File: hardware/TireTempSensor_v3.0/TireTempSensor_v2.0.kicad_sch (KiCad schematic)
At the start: 36 parts, among them J1 SWD_01x06, J2 CAN_01x04, SW1 RESET, SW2 3 pos dip switch, U1 STM32G0C1KCTxN, Y1 16MGHz

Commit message: Piotruś prosił :3
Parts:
- removed J1: SWD_01x06, Connector_PinHeader_2.54mm:PinHeader_1x06_P2.54mm_Vertical, symbol Connector_Generic:Conn_01x06
- added J3: FTSH-107-01-L-D-K, Samacsys:FTSH-107-XX-YYY-D-K, symbol Samacsys_kicad_sym:FTSH-107-01-L-D-K
- D1: value D_Zener -> 30V; footprint (none) -> Diode_SMD:D_SOD-123
- D10, D7, D8, D9: footprint (none) -> Package_TO_SOT_SMD:SOT-23_Handsoldering
- D11, D12: footprint (none) -> Diode_SMD:D_SOD-123
- SW2: footprint (none) -> footprint:DS04254103BKSMT
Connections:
- net GND: now also J3.11 (Pin_11), J3.5 (Pin_5), J3.7 (Pin_7); no longer D9.3 (common)
- net NRST: now also J3.12 (Pin_12)
- net SWCLK: now also J3.6 (Pin_6)
- net SWDIO: now also J3.4 (Pin_4)
- net SWO: now also J3.8 (Pin_8)
- new net +3.3V: J3.3 (Pin_3)
- new net GND_ISO: D9.3 (common)
- no-connect marks 1 -> 6
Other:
- moved on the sheet: J2

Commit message: Poprawki, kontynuacja layoutu
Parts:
- removed C16: 100n, Capacitor_SMD:C_0603_1608Metric, symbol Device:C_Small
- removed D10, D7, D8, D9: D_TVS_Dual_AAC, Package_TO_SOT_SMD:SOT-23_Handsoldering, symbol Device:D_TVS_Dual_AAC
- removed R17: 10k, Resistor_SMD:R_0603_1608Metric, symbol Device:R_Small_US
- removed R20: 1k, Resistor_SMD:R_0603_1608Metric, symbol Device:R_Small_US
- removed SW2: 3 pos dip switch, footprint:DS04254103BKSMT, symbol Switch:SW_DIP_x03
- added SW3: SW_DIP_x02, footprint:2192LPST, symbol Switch:SW_DIP_x02
- J2: value CAN_01x04 -> Main connector; footprint Connector_Wire:SolderWire-0.1sqmm_1x04_P3.6mm_D0.4mm_OD1mm_Relief -> footprint:M80-51004YY
- J3: footprint Samacsys:FTSH-107-XX-YYY-D-K -> footprint:FTSH-107-XX-YYY-DV-K
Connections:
- net Switch3 is gone; now on net CAN RX: U1.22 (PA11/PA9)
- net CAN +: now also J2.4 (Pin_4); no longer J2.3 (Pin_3)
- net CAN -: now also J2.3 (Pin_3); no longer J2.4 (Pin_4)
- net CAN TX: now also U1.1 (PB9)
- net LED ERR: now also U1.11 (PA4); no longer U1.13 (PA6)
- net LED OK: now also U1.10 (PA3); no longer U1.12 (PA5)
- net LED WAR1: now also U1.12 (PA5); no longer U1.14 (PA7)
- net LED WAR2: now also U1.13 (PA6); no longer U1.18 (PA8)
- net Switch1: now also SW3.1
- net Switch2: now also SW3.2
- net at R19.1: now also SW3.3
- net at R18.1: now also SW3.4
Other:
- added sheet ESD_Protection (ESD_Protection.kicad_sch)
- note added: "Dla 4 czujników wystarczą 2 pozycje adresy 0-3"
- note removed: "ESD Protection"
- moved on the sheet: C12, C13, J2, R15, R16, R18, R19, U1

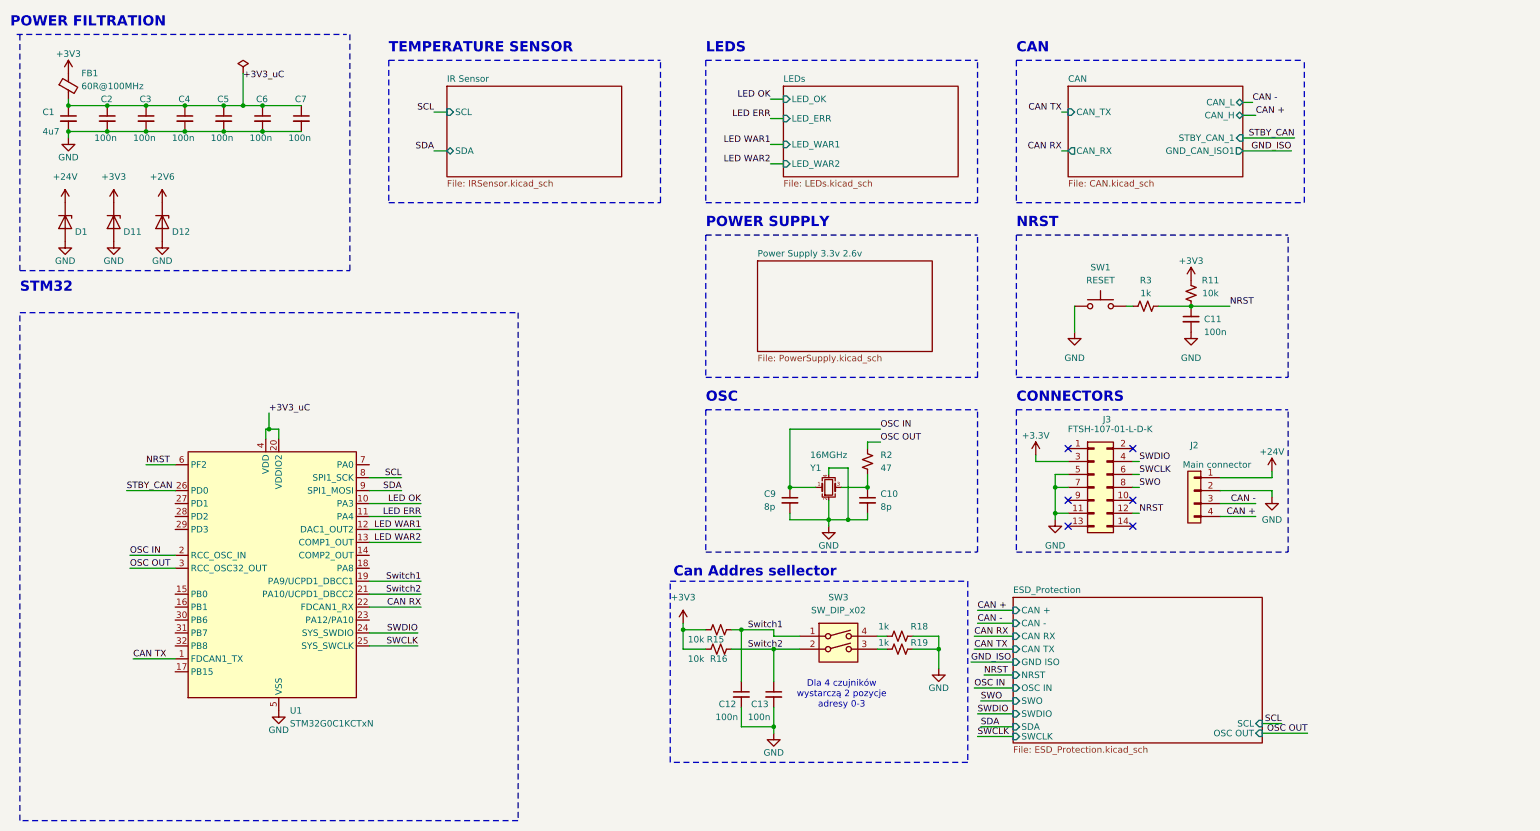
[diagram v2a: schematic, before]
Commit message: Nowy layout, nowe tvsy
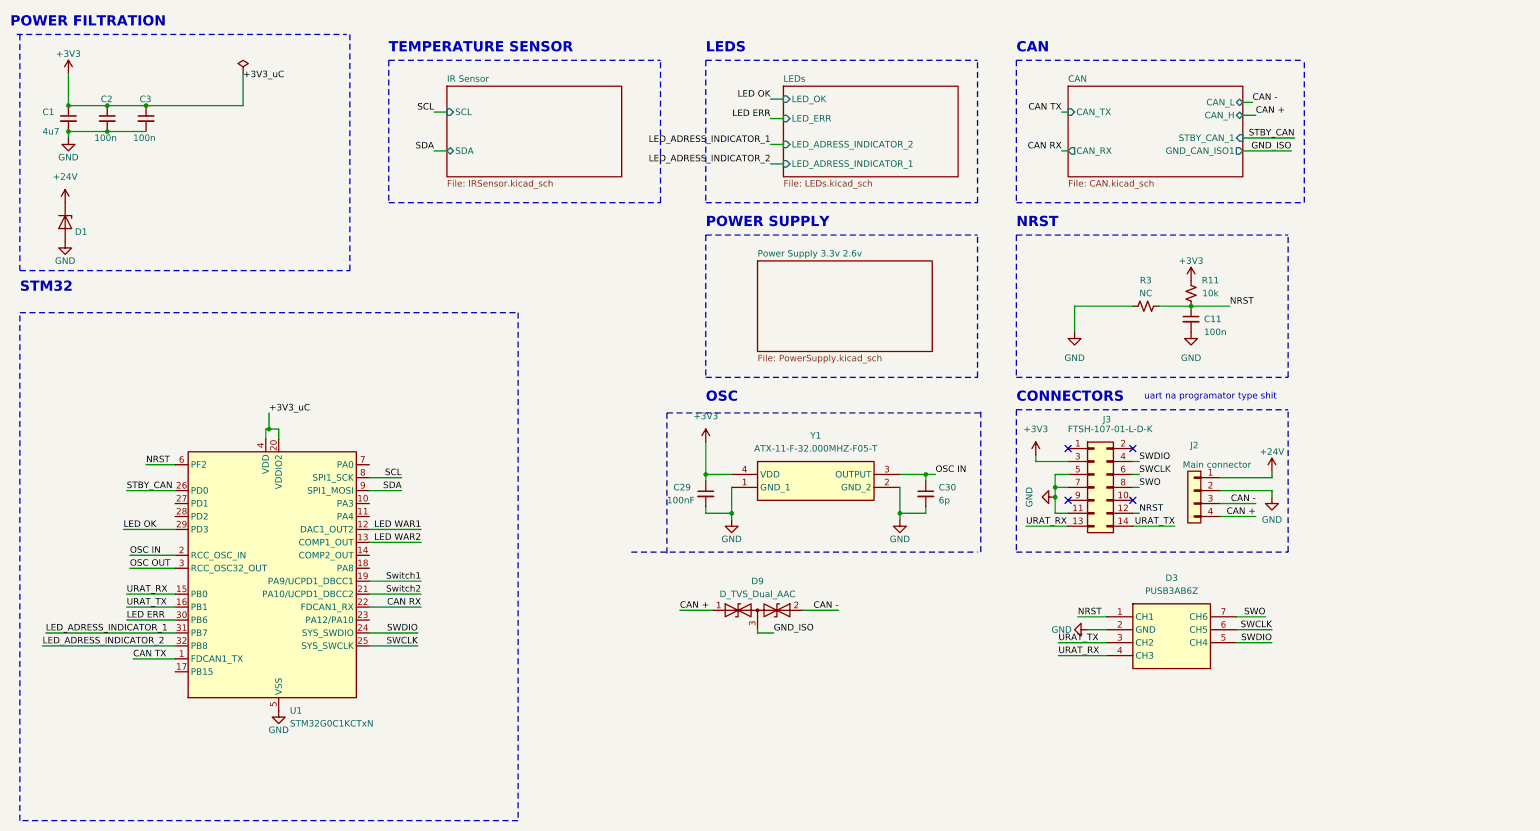
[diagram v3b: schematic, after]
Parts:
- removed C10, C9: 8p, Capacitor_SMD:C_0603_1608Metric, symbol Device:C_Small
- removed C12, C13, C4, C5, C6, C7: 100n, Capacitor_SMD:C_0603_1608Metric, symbol Device:C_Small
- removed D11, D12: D_Zener, Diode_SMD:D_SOD-123, symbol Device:D_Zener
- removed FB1: 60R@100MHz, Inductor_SMD:L_0603_1608Metric, symbol Device:FerriteBead_Small
- removed R15, R16: 10k, Resistor_SMD:R_0603_1608Metric, symbol Device:R_Small_US
- removed R18, R19: 1k, Resistor_SMD:R_0603_1608Metric, symbol Device:R_Small_US
- removed R2: 47, Resistor_SMD:R_0603_1608Metric, symbol Device:R_Small_US
- removed SW1: RESET, Button:PTS815SJK250SMTRLFS, symbol Switch:SW_MEC_5G
- removed SW3: SW_DIP_x02, footprint:2192LPST, symbol Switch:SW_DIP_x02
- removed Y1: 16MGHz, Crystal:Crystal_SMD_SeikoEpson_TSX3225-4Pin_3.2x2.5mm, symbol Device:Crystal_GND24_Small
- added C29: 100nF, Capacitor_SMD:C_0603_1608Metric_Pad1.08x0.95mm_HandSolder, symbol Device:C_Small
- added C30: 6p, Capacitor_SMD:C_0603_1608Metric_Pad1.08x0.95mm_HandSolder, symbol Device:C_Small
- added D3: PUSB3AB6Z, footprint:PUSB3AB6Z, symbol PUSB3AB6Z:PUSB3AB6Z
- added D9: D_TVS_Dual_AAC, Package_TO_SOT_SMD:SOT-23_Handsoldering, symbol Device:D_TVS_Dual_AAC
- added Y1: ATX-11-F-32.000MHZ-F05-T, footprint:ATX11F32000MHZF05T, symbol Samacsys:ATX-11-F-32.000MHZ-F05-T
- R3: value 1k -> NC; footprint Resistor_SMD:R_0603_1608Metric -> Resistor_SMD:R_0201_0603Metric
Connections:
- net +3.3V is gone; now on net +3V3: J3.3 (Pin_3)
- net +3V3_uC is gone; now on net +3V3: C1.1, C2.1, C3.1, U1.20 (VDDIO2), U1.4 (VDD)
- net +3V3: now also C29.1, Y1.4 (VDD)
- net CAN +: now also D9.1 (A1)
- net CAN -: now also D9.2 (A2)
- net GND: now also R3.1, C29.2, C30.2, D3.2 (GND), Y1.1 (GND_1), Y1.2 (GND_2)
- net GND_ISO: now also D9.3 (common)
- net LED ERR: now also U1.30 (PB6); no longer U1.11 (PA4)
- net LED OK: now also U1.29 (PD3); no longer U1.10 (PA3)
- net NRST: now also D3.1 (CH1)
- net OSC IN: now also C30.1, Y1.3 (OUTPUT)
- net SWCLK: now also D3.6 (CH5)
- net SWDIO: now also D3.5 (CH4)
- net SWO: now also D3.7 (CH6)
- net URAT_RX: now reaches U1.15 (PB0)
- net URAT_RX: now also J3.13 (Pin_13), D3.4 (CH3)
- net URAT_TX: now reaches U1.16 (PB1)
- net URAT_TX: now also J3.14 (Pin_14), D3.3 (CH2)
- net LED_ADRESS_INDICATOR_1: now reaches U1.31 (PB7)
- net LED_ADRESS_INDICATOR_2: now reaches U1.32 (PB8)
- no-connect marks 6 -> 4
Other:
- removed sheet ESD_Protection
- sheet LEDs ports: added LED_ADRESS_INDICATOR_1, LED_ADRESS_INDICATOR_2; removed LED_WAR1, LED_WAR2
- note added: "uart na programator type shit"
- note removed: "Can Addres sellector"
- note removed: "Dla 4 czujników wystarczą 2 pozycje adresy 0-3"

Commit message: Gotowe do sprawdzenia
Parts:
- R3: footprint Resistor_SMD:R_0201_0603Metric -> Resistor_SMD:R_0402_1005Metric
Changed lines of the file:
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@@
 			)
 		)
-		(property "Footprint" "Resistor_SMD:R_0201_0603Metric"
+		(property "Footprint" "Resistor_SMD:R_0402_1005Metric"
 			(at 248.92 73.66 0)
 			(effects

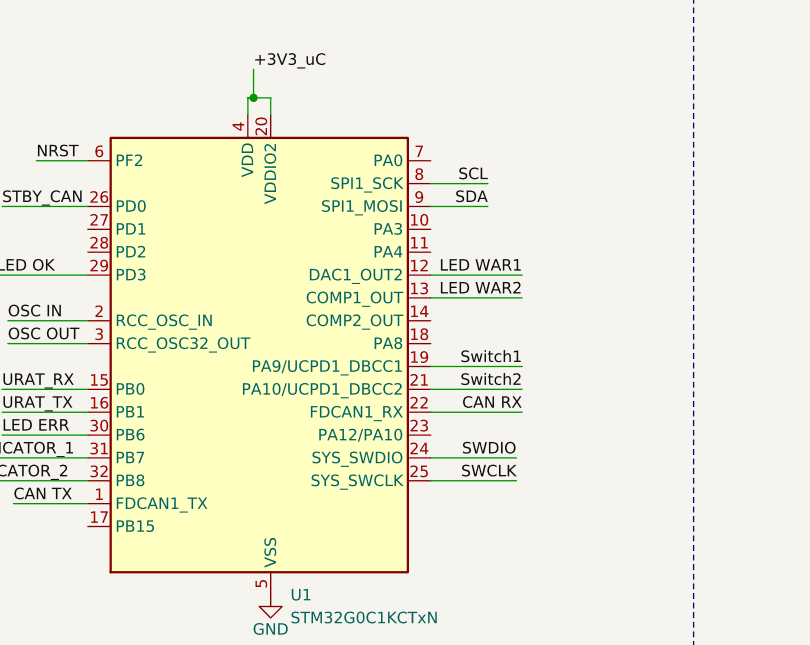
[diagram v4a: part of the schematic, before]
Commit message: Poprawiono SPI NA I2C
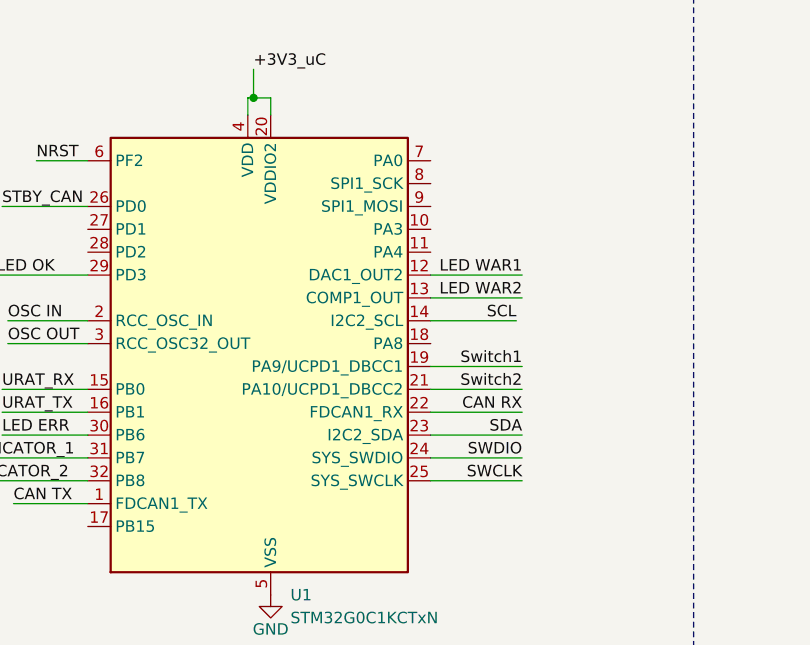
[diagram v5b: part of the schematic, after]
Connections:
- net SCL: now also U1.14 (PA7); no longer U1.8 (PA1)
- net SDA: now also U1.23 (PA12/PA10); no longer U1.9 (PA2)
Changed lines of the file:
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@@
 	(wire
 		(pts
-			(xy 96.52 137.795) (xy 106.045 137.795)
-		)
-		(stroke
-			(width 0)
-			(type default)
-		)
-	)
-	(wire
-		(pts
-			(xy 96.52 107.315) (xy 102.87 107.315)
+			(xy 96.52 137.795) (xy 106.68 137.795)
 		)
 		(stroke
@@
 	(wire
 		(pts
+			(xy 96.52 122.555) (xy 106.045 122.555)
+		)
+		(stroke
+			(width 0)
+			(type default)
+		)
+	)
+	(wire
+		(pts
 			(xy 246.38 114.3) (xy 247.65 114.3)
 		)
@@
 		)
 	)
+	(wire
+		(pts
+			(xy 96.52 135.255) (xy 106.68 135.255)
+		)
+		(stroke
+			(width 0)
+			(type default)
+		)
+	)
 	(polyline
 		(pts
@@
 	(wire
 		(pts
-			(xy 96.52 140.335) (xy 106.045 140.335)
+			(xy 96.52 140.335) (xy 106.68 140.335)
 		)
 		(stroke
@@
 		(pts
 			(xy 172.72 137.795) (xy 172.72 137.16)
-		)
-		(stroke
-			(width 0)
-			(type default)
-		)
-	)
-	(wire
-		(pts
-			(xy 96.52 109.855) (xy 102.87 109.855)
 		)
 		(stroke
@@
 	)
 	(label "SWCLK"
-		(at 106.045 140.335 180)
+		(at 106.68 140.335 180)
 		(effects
 			(font
@@
 	)
 	(label "SDA"
-		(at 102.87 109.855 180)
+		(at 106.68 135.255 180)
 		(effects
 			(font
@@
 	)
 	(label "SCL"
-		(at 102.87 107.315 180)
+		(at 106.045 122.555 180)
 		(effects
 			(font
@@
 	)
 	(label "SWDIO"
-		(at 106.045 137.795 180)
+		(at 106.68 137.795 180)
 		(effects
 			(font
@@
 		)
 		(pin "14"
-			(alternate "COMP2_OUT")
+			(alternate "I2C2_SCL")
 		)
 		(pin "23"
+			(alternate "I2C2_SDA")
 		)
 		(pin "2"

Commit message: Poprawione :3
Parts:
- added D7, D8: Quad TVS, SOT95P285X140-6N, symbol D5V0P4UR6SO-7:D5V0P4UR6SO-7
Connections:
- net +3V3: now also D8.3 (I/O2)
- net GND: now also D7.2 (VSS), D7.5 (VCC), D8.2 (VSS), D8.5 (VCC); no longer D3.2 (GND)
- net NRST: now also D7.1 (I/O1); no longer D3.1 (CH1)
- net SWCLK: now also D7.6 (I/O4); no longer D3.6 (CH5)
- net SWDIO: now also D7.4 (I/O3); no longer D3.5 (CH4)
- net SWO: now also D7.3 (I/O2); no longer D3.7 (CH6)
- net URAT_RX: now also D8.6 (I/O4); no longer D3.4 (CH3)
- net URAT_TX: now also D8.4 (I/O3); no longer D3.3 (CH2)
- no-connect marks 4 -> 5

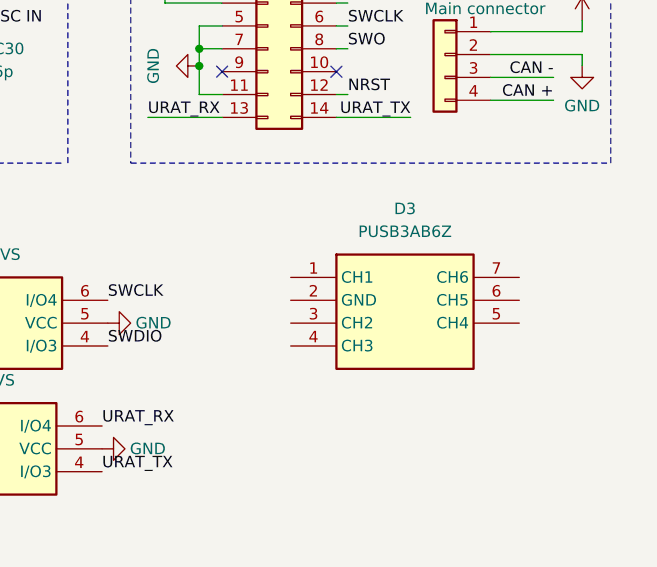
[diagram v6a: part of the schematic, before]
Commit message: Zmieniono routing w celu zmniejszenia przecięć masy
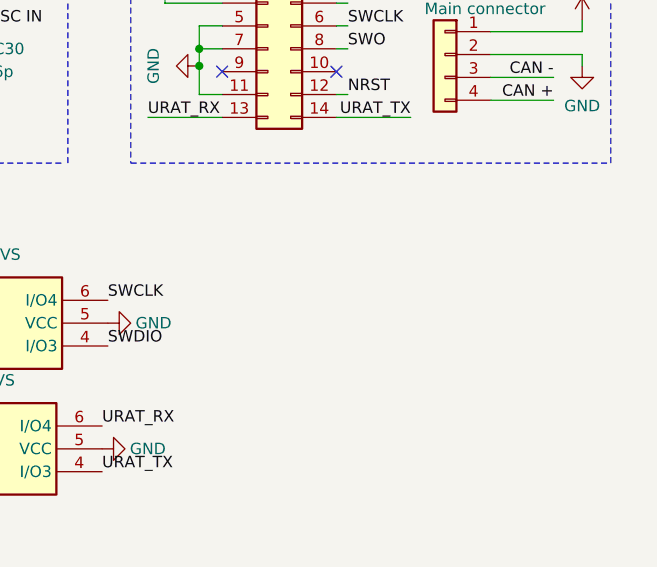
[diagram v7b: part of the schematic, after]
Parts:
- removed D3: PUSB3AB6Z, footprint:PUSB3AB6Z, symbol PUSB3AB6Z:PUSB3AB6Z
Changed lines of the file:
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@@
-	)
-	(symbol
-		(lib_id "PUSB3AB6Z:PUSB3AB6Z")
-		(at 241.3 134.62 0)
-		(unit 1)
-		(exclude_from_sim no)
-		(in_bom yes)
-		(on_board yes)
-		(dnp no)
-		(fields_autoplaced yes)
-		(property "Reference" "D3"
-			(at 254 127 0)
-			(effects
-				(font
-					(size 1.27 1.27)
-				)
-			)
-		)
-		(property "Value" "PUSB3AB6Z"
-			(at 254 129.54 0)
-			(effects
-				(font
-					(size 1.27 1.27)
-				)
-			)
-		)
-		(property "Footprint" "footprint:PUSB3AB6Z"
-			(at 262.89 229.54 0)
-			(effects
-				(font
-					(size 1.27 1.27)
-				)
-				(justify left top)
-				(hide yes)
-			)
-		)
-		(property "Datasheet" "https://assets.nexperia.com/documents/data-sheet/PUSB3AB6.pdf"
-			(at 262.89 329.54 0)
-			(effects
-				(font
-					(size 1.27 1.27)
-				)
-				(justify left top)
-				(hide yes)
-			)
-		)
-		(property "Description" "Nexperia PUSB3AB6Z, Hex-Element ESD Protection Diode, 7-Pin DFN2111"
-			(at 241.3 134.62 0)
-			(effects
-				(font
-					(size 1.27 1.27)
-				)
-				(hide yes)
-			)
-		)
-		(property "Height" "0.5"
-			(at 262.89 529.54 0)
-			(effects
-				(font
-					(size 1.27 1.27)
-				)
-				(justify left top)
-				(hide yes)
-			)
-		)
-		(property "Mouser Part Number" "771-PUSB3AB6Z"
-			(at 262.89 629.54 0)
-			(effects
-				(font
-					(size 1.27 1.27)
-				)
-				(justify left top)
-				(hide yes)
-			)
-		)
-		(property "Mouser Price/Stock" "https://www.mouser.co.uk/ProductDetail/Nexperia/PUSB3AB6Z?qs=K2OaAKmNuLgoMk8bcuWLKw%3D%3D"
-			(at 262.89 729.54 0)
-			(effects
-				(font
-					(size 1.27 1.27)
-				)
-				(justify left top)
-				(hide yes)
-			)
-		)
-		(property "Manufacturer_Name" "Nexperia"
-			(at 262.89 829.54 0)
-			(effects
-				(font
-					(size 1.27 1.27)
-				)
-				(justify left top)
-				(hide yes)
-			)
-		)
-		(property "Manufacturer_Part_Number" "PUSB3AB6Z"
-			(at 262.89 929.54 0)
-			(effects
-				(font
-					(size 1.27 1.27)
-				)
-				(justify left top)
-				(hide yes)
-			)
-		)
-		(pin "5"
-		)
-		(pin "4"
-		)
-		(pin "3"
-		)
-		(pin "7"
-		)
-		(pin "6"
-		)
-		(pin "1"
-		)
-		(pin "2"
-		)
-		(instances
-			(project ""
-				(path "/6e95e1be-fdd6-40ae-a4f8-5c53e6058d6c"
-					(reference "D3")
-					(unit 1)
-				)
-			)
-		)
 	)
 	(symbol

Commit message: Piotrkowe poprawy
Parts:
- added TP3: TestPoint_Small, TestPoint:TestPoint_Pad_D1.0mm, symbol Connector:TestPoint_Small
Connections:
- net OSC IN: now also TP3.1
- net CAN + renamed CAN+
- net CAN - renamed CAN-
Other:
- note added: "ESD protection"
- note removed: "uart na programator type shit"
- moved on the sheet: D7, D8, D9
